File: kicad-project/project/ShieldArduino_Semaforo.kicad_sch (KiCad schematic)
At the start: 65 parts, among them IC2 TPS563200DDCR, J1 Conn_01x15, K1 RELAY, P1 Power, P2 Analog, P3 Digital, P4 Digital, P5 CONN_01X01, P6 CONN_01X01, P7 CONN_01X01, P8 CONN_01X01, Q1 PMOS, Q2 NMOS, Q3 NMOS, Q4 NMOS, Q5 NMOS, U1 MCP2542FD-E/MF, U2 LM321

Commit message: kicad-pcb-layout-v1.0
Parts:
- removed J1: Conn_01x15, footprint:L17HTHES4R1C, symbol Connector_Generic:Conn_01x15
- added J2: Conn_01x18, footprint:M80-54016YY, symbol Connector_Generic:Conn_01x18
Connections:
- net  relay_in: now also J2.6 (Pin_6)
- net +5V: now also J2.13 (Pin_13), J2.16 (Pin_16)
- net 12V_in: now also J2.1 (Pin_1)
- net EX_CAN+: now also J2.7 (Pin_7)
- net EX_CAN-: now also J2.8 (Pin_8)
- net GND: now also J2.10 (Pin_10), J2.15 (Pin_15), J2.17 (Pin_17), J2.18 (Pin_18), J2.9 (Pin_9)
- net brake_in: now also J2.14 (Pin_14)
- net high_speed: now also J2.12 (Pin_12)
- net inverter_signal_5V: now also J2.5 (Pin_5)
- net low_speed: now also J2.4 (Pin_4)
- net relay_out: now also J2.2 (Pin_2)
- net reverse: now also J2.3 (Pin_3)
- net throttle_in: now also J2.11 (Pin_11)
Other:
- moved on the sheet: D1, D11, D12, D13, D2, D3, D4

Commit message: kicad-pcb-layout-v1.0.1
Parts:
- added C3: 100n, Capacitor_SMD:C_0805_2012Metric_Pad1.18x1.45mm_HandSolder, symbol Device:C_Small
- added C5: 220p, Capacitor_SMD:C_0805_2012Metric_Pad1.18x1.45mm_HandSolder, symbol Device:C_Small
- added D6: D_Small, footprint:SODFL3618X100N, symbol Device:D_Small
- added IC1: TLIN1039DDFRQ1, SOT65P280X110-8N, symbol TLIN1039DDFRQ1:TLIN1039DDFRQ1
- added R12: 10k, Resistor_SMD:R_0805_2012Metric_Pad1.20x1.40mm_HandSolder, symbol Device:R_Small
- added R13: 1k, Resistor_SMD:R_0805_2012Metric_Pad1.20x1.40mm_HandSolder, symbol Device:R_Small
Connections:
- net +3V3: now also R12.1
- net 12V_in_protected: now also C3.1, D6.2 (A), IC1.7 (VSUP)
- net A4(SDA): now also J2.17 (Pin_17)
- net A5(SCL): now also J2.18 (Pin_18)
- net GND: now also C3.2, C5.2, IC1.5 (GND); no longer J2.15 (Pin_15), J2.17 (Pin_17), J2.18 (Pin_18)
- net UART_RX: now also IC1.4 (TXD)
- net UART_TX: now also IC1.1 (RXD)
- new net: IC1.2 (EN), R12.2
- new net: D6.1 (K), R13.1
- new net TLIN: C5.1, IC1.6 (LIN), J2.15 (Pin_15), R13.2
- no-connect marks 5 -> 7

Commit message: kicad-pcb-layout-v1.0.2
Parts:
- removed R14, R16: 10k, Resistor_SMD:R_0603_1608Metric_Pad0.98x0.95mm_HandSolder, symbol Device:R_Small
- removed R19: 5.2K, Resistor_SMD:R_0603_1608Metric_Pad0.98x0.95mm_HandSolder, symbol Device:R_Small
- removed U2: LM321, Package_TO_SOT_SMD:SOT-23-5, symbol Amplifier_Operational:LM321
- added C6: 100n, Capacitor_SMD:C_0805_2012Metric_Pad1.18x1.45mm_HandSolder, symbol Device:C_Small
- added IC3: MCP4901T-E_MS, SOP65P490X110-8N, symbol MCP4901T-E_MS:MCP4901T-E_MS
- added JP1: Jumper_2_Small_Bridged, symbol Jumper:Jumper_2_Small_Bridged
- added JP2: Jumper_2_Small_Open, symbol Jumper:Jumper_2_Small_Open
- added R21: 200, Resistor_SMD:R_0603_1608Metric_Pad0.98x0.95mm_HandSolder, symbol Device:R_Small
- added R22, R23: 5k, Resistor_SMD:R_0603_1608Metric_Pad0.98x0.95mm_HandSolder, symbol Device:R_Small
- added U3: LM4040DBZ-2.0, Package_TO_SOT_SMD:SOT-23, symbol Reference_Voltage:LM4040DBZ-2.0
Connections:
- net +3V3: now also R23.1
- net +5V: now also C6.1, IC3.1 (VDD)
- net 11(**/MOSI): now also IC3.4 (SDI)
- net 13(SCK): now also IC3.3 (SCK)
- net AREF: now also JP2.2 (B)
- net GND: now also C6.2, IC3.7 (VSS), R21.2, R22.2, U3.2 (A)
- net inverter_signal_5V: now also IC3.8 (VOUT)
- net 6(**) renamed STM_DAC_IN
- net STM_DAC_IN: now also IC3.2 (~{CS}), R21.1
- net 7 renamed STM_LDAC
- net STM_LDAC: now also IC3.5 (~{LDAC}), R22.1
- new net: IC3.6 (VREF), JP1.1 (A), JP2.1 (A)
- new net: JP1.2 (B), R23.2, U3.1 (K)
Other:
- note added: "DAC"
- note added: "PEDALS"
- note added: "TLIN"
- note removed: "OPAMP_ENG"
- note removed: "PEDAL"
- moved on the sheet: C3, C5, C7, D6, F2, IC1, P1, P2, P3, P4, P5, P6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

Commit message: kicad-pcb-layout-v1.0.4
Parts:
- JP1: footprint (none) -> Jumper:SolderJumper-2_P1.3mm_Bridged_RoundedPad1.0x1.5mm
- JP2: footprint (none) -> Jumper:SolderJumper-2_P1.3mm_Open_RoundedPad1.0x1.5mm
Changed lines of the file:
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@@
 		(on_board yes)
 		(dnp no)
-		(fields_autoplaced yes)
 		(property "Reference" "R23"
 			(at 218.44 41.9099 0)
@@
 			)
 		)
-		(property "Footprint" ""
+		(property "Footprint" "Jumper:SolderJumper-2_P1.3mm_Open_RoundedPad1.0x1.5mm"
 			(at 200.66 64.77 0)
 			(effects
@@
 			)
 		)
-		(property "Footprint" ""
+		(property "Footprint" "Jumper:SolderJumper-2_P1.3mm_Bridged_RoundedPad1.0x1.5mm"
 			(at 200.66 49.53 0)
 			(effects

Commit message: kicad-pcb-layout-v1.0.7
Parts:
- removed F2: 0.5A, Fuse:Fuse_1206_3216Metric_Pad1.42x1.75mm_HandSolder, symbol Device:Fuse_Small
- added F1: 3A, Fuse:Fuse_0603_1608Metric_Pad1.05x0.95mm_HandSolder, symbol Device:Fuse_Small
- D16: footprint Diode_SMD:D_SOD-323F -> Diode_SMD:D_SOD-323_HandSoldering
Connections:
- net 12V_in_protected: now also F1.2
- net at D9.1 (K), Q1.3 (S): now also F1.1
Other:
- note added: "current limiting resistor"
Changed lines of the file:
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@@
 		)
 	)
+	(text "current limiting resistor"
+		(exclude_from_sim no)
+		(at 202.692 180.34 0)
+		(effects
+			(font
+				(face "Calibri")
+				(size 1.016 1.016)
+			)
+		)
+	)
 	(text "1"
 		(exclude_from_sim no)
@@
 		)
 	)
+	(text "current limiting resistor"
+		(exclude_from_sim no)
+		(at 274.828 176.276 0)
+		(effects
+			(font
+				(face "Calibri")
+				(size 1.016 1.016)
+			)
+		)
+	)
 	(text "POWER SUPPLY UNIT"
 		(exclude_from_sim no)
@@
 		)
 	)
+	(text "current limiting resistor"
+		(exclude_from_sim no)
+		(at 125.984 180.594 0)
+		(effects
+			(font
+				(face "Calibri")
+				(size 1.016 1.016)
+			)
+		)
+	)
 	(text "CAN\n"
 		(exclude_from_sim no)
@@
 			)
 		)
-		(property "Footprint" "Diode_SMD:D_SOD-323F"
+		(property "Footprint" "Diode_SMD:D_SOD-323_HandSoldering"
 			(at 44.45 127 0)
 			(effects
@@
 	)
 	(symbol
+		(lib_id "Device:Fuse_Small")
+		(at 64.77 66.04 0)
+		(unit 1)
+		(exclude_from_sim no)
+		(in_bom yes)
+		(on_board yes)
+		(dnp no)
+		(fields_autoplaced yes)
+		(property "Reference" "F1"
+			(at 64.77 60.96 0)
+			(effects
+				(font
+					(size 1.27 1.27)
+				)
+				(hide yes)
+			)
+		)
+		(property "Value" "3A"
+			(at 64.77 63.5 0)
+			(effects
+				(font
+					(size 1.27 1.27)
+				)
+			)
+		)
+		(property "Footprint" "Fuse:Fuse_0603_1608Metric_Pad1.05x0.95mm_HandSolder"
+			(at 64.77 66.04 0)
+			(effects
+				(font
+					(size 1.27 1.27)
+				)
+				(hide yes)
+			)
+		)
+		(property "Datasheet" "https://www.mouser.pl/ProductDetail/Bourns/SF-0603FP300F-2?qs=55YtniHzbhAz28pQ%252B5v2Gg%3D%3D"
+			(at 64.77 66.04 0)
+			(effects
+				(font
+					(size 1.27 1.27)
+				)
+				(hide yes)
+			)
+		)
+		(property "Description" "Fuse, small symbol"
+			(at 64.77 66.04 0)
+			(effects
+				(font
+					(size 1.27 1.27)
+				)
+				(hide yes)
+			)
+		)
+		(pin "1"
+		)
+		(pin "2"
+		)
+		(instances
+			(project "ShieldArduino_Semaforo"
+				(path "/9ffb0a36-b6c4-4251-92f7-01d561ef1727"
+					(reference "F1")
+					(unit 1)
+				)
+			)
+		)
+	)
+	(symbol
 		(lib_id "Device:R_Small")
 		(at 76.2 34.29 0)
@@
 					(unit 1)
 				)
-			)
-		)
-	)
-	(symbol
-		(lib_id "Device:Fuse_Small")
-		(at 64.77 66.04 0)
-		(unit 1)
-		(exclude_from_sim no)
-		(in_bom yes)
-		(on_board yes)
-		(dnp no)
-		(fields_autoplaced yes)
-		(property "Reference" "F2"
-			(at 64.77 60.96 0)
-			(effects
-				(font
-					(size 1.27 1.27)
-				)
-			)
-		)
-		(property "Value" "0.5A"
-			(at 64.77 63.5 0)
-			(effects
-				(font
-					(size 1.27 1.27)
-				)
-			)
-		)
-		(property "Footprint" "Fuse:Fuse_1206_3216Metric_Pad1.42x1.75mm_HandSolder"
-			(at 64.77 66.04 0)
-			(effects
-				(font
-					(size 1.27 1.27)
-				)
-				(hide yes)
-			)
-		)
-		(property "Datasheet" "https://www.mouser.pl/ProductDetail/Eaton-Electronics/PTSAHT120624V050?qs=sGAEpiMZZMt8Ji9PfVTQzDC%2FQhf%2F9COsTqlHB7vDZt22fVe0wfbojQ%3D%3D"
-			(at 64.77 66.04 0)
-			(effects
-				(font
-					(size 1.27 1.27)
-				)
-				(hide yes)
-			)
-		)
-		(property "Description" "Fuse, small symbol"
-			(at 64.77 66.04 0)
-			(effects
-				(font
-					(size 1.27 1.27)
-				)
-				(hide yes)
-			)
-		)
-		(pin "1"
-		)
-		(pin "2"
-		)
-		(instances
-			(project "ShieldArduino_Semaforo"
-				(path "/9ffb0a36-b6c4-4251-92f7-01d561ef1727"
-					(reference "F2")
-					(unit 1)
-				)

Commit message: kicad-pcb-layout-v1.0.8
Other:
- note added: "PSU: PRZED PRZETWORNICA 1A BEZPIECZNIK"
- note added: "TVS: DODAĆ TVS NA I2C"
- note removed: "FARDRIVER: jakie piny potrzeba,do czego podłączać = ile tranzystorów bezpiecznik topikowy na zasilanie przekaźników/przekaźników przekaznik ON/OFF tranzystor REVERSE tranzystor 3 grade speed (highspeed, medium speed, lowspeed)"
- note removed: "PSU: ułożyć zasilacz tak jak na layout example (click+D) CHYBA GIT POTWIERDZIC Z WIKTOREM <3"
- note removed: "TVS: kazdy pinout musi miec tvs dobranego na working voltage +0.5V"
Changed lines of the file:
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@@
 		)
 	)
-	(text "PSU:\n	ułożyć zasilacz tak jak na layout example (click+D)\n	CHYBA GIT POTWIERDZIC Z WIKTOREM <3"
+	(text "PSU:\n	PRZED PRZETWORNICA 1A BEZPIECZNIK\n"
 		(exclude_from_sim no)
-		(at 17.78 -17.526 0)
+		(at 20.574 -26.416 0)
 		(effects
 			(font
@@
 		)
 	)
-	(text "FARDRIVER:\n	jakie piny potrzeba,do czego podłączać = ile tranzystorów\n	bezpiecznik topikowy na zasilanie przekaźników/przekaźników\n 	przekaznik ON/OFF\n	tranzystor REVERSE\n	tranzystor 3 grade speed (highspeed, medium speed, lowspeed)\n \n\n"
-		(exclude_from_sim no)
-		(at 17.78 -30.48 0)
-		(effects
-			(font
-				(size 1.27 1.27)
-			)
-			(justify left)
-		)
-	)
 	(text "ESD PROTECTION\n"
 		(exclude_from_sim no)
@@
 		)
 	)
-	(text "TVS:\n	kazdy pinout musi miec tvs dobranego na working voltage +0.5V\n\n"
+	(text "TVS:\n	DODAĆ TVS NA I2C\n\n"
 		(exclude_from_sim no)
-		(at 18.034 -22.606 0)
+		(at 20.828 -31.496 0)
 		(effects
 			(font
@@
 	(wire
 		(pts
-			(xy 134.62 186.69) (xy 134.62 187.96)
-		)
-		(stroke
-			(width 0)
-			(type default)
-		)
-	)
-	(wire
-		(pts
 			(xy 275.59 166.37) (xy 283.21 166.37)
 		)
@@
 	(symbol
 		(lib_id "power:GND")
-		(at 134.62 187.96 0)
+		(at 134.62 186.69 0)
 		(unit 1)
 		(exclude_from_sim no)
@@
 		(dnp no)
 		(property "Reference" "#PWR024"
-			(at 134.62 194.31 0)
+			(at 134.62 193.04 0)
 			(effects
 				(font
@@
 		)
 		(property "Value" "GND"
-			(at 134.874 192.532 0)
+			(at 134.874 191.262 0)
 			(effects
 				(font
@@
 		)
 		(property "Footprint" ""
-			(at 134.62 187.96 0)
+			(at 134.62 186.69 0)
 			(effects
 				(font
@@
 		)
 		(property "Datasheet" ""
-			(at 134.62 187.96 0)
+			(at 134.62 186.69 0)
 			(effects
 				(font
@@
 		)
 		(property "Description" "Power symbol creates a global label with name \"GND\" , ground"
-			(at 134.62 187.96 0)
+			(at 134.62 186.69 0)
 			(effects
 				(font

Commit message: kicad-pcb-layout-v1.0.9
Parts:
- added C8: 100n, Capacitor_SMD:C_0805_2012Metric_Pad1.18x1.45mm_HandSolder, symbol Device:C_Small
- added R14: 5k, Resistor_SMD:R_0603_1608Metric_Pad0.98x0.95mm_HandSolder, symbol Device:R_Small
- added R16: 10k, Resistor_SMD:R_0603_1608Metric_Pad0.98x0.95mm_HandSolder, symbol Device:R_Small
- added R19: 200, Resistor_SMD:R_0603_1608Metric_Pad0.98x0.95mm_HandSolder, symbol Device:R_Small
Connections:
- net A3: now also C8.1, R19.2
- net GND: now also C8.2, R16.2
- net inverter_signal_5V: now also R14.1
- new net: R14.2, R16.1, R19.1
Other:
- note added: "PSU: PRZED PRZETWORNICA 1A BEZPIECZNIK DAC: CZY A3 pin git?"
- note removed: "PSU: PRZED PRZETWORNICA 1A BEZPIECZNIK"

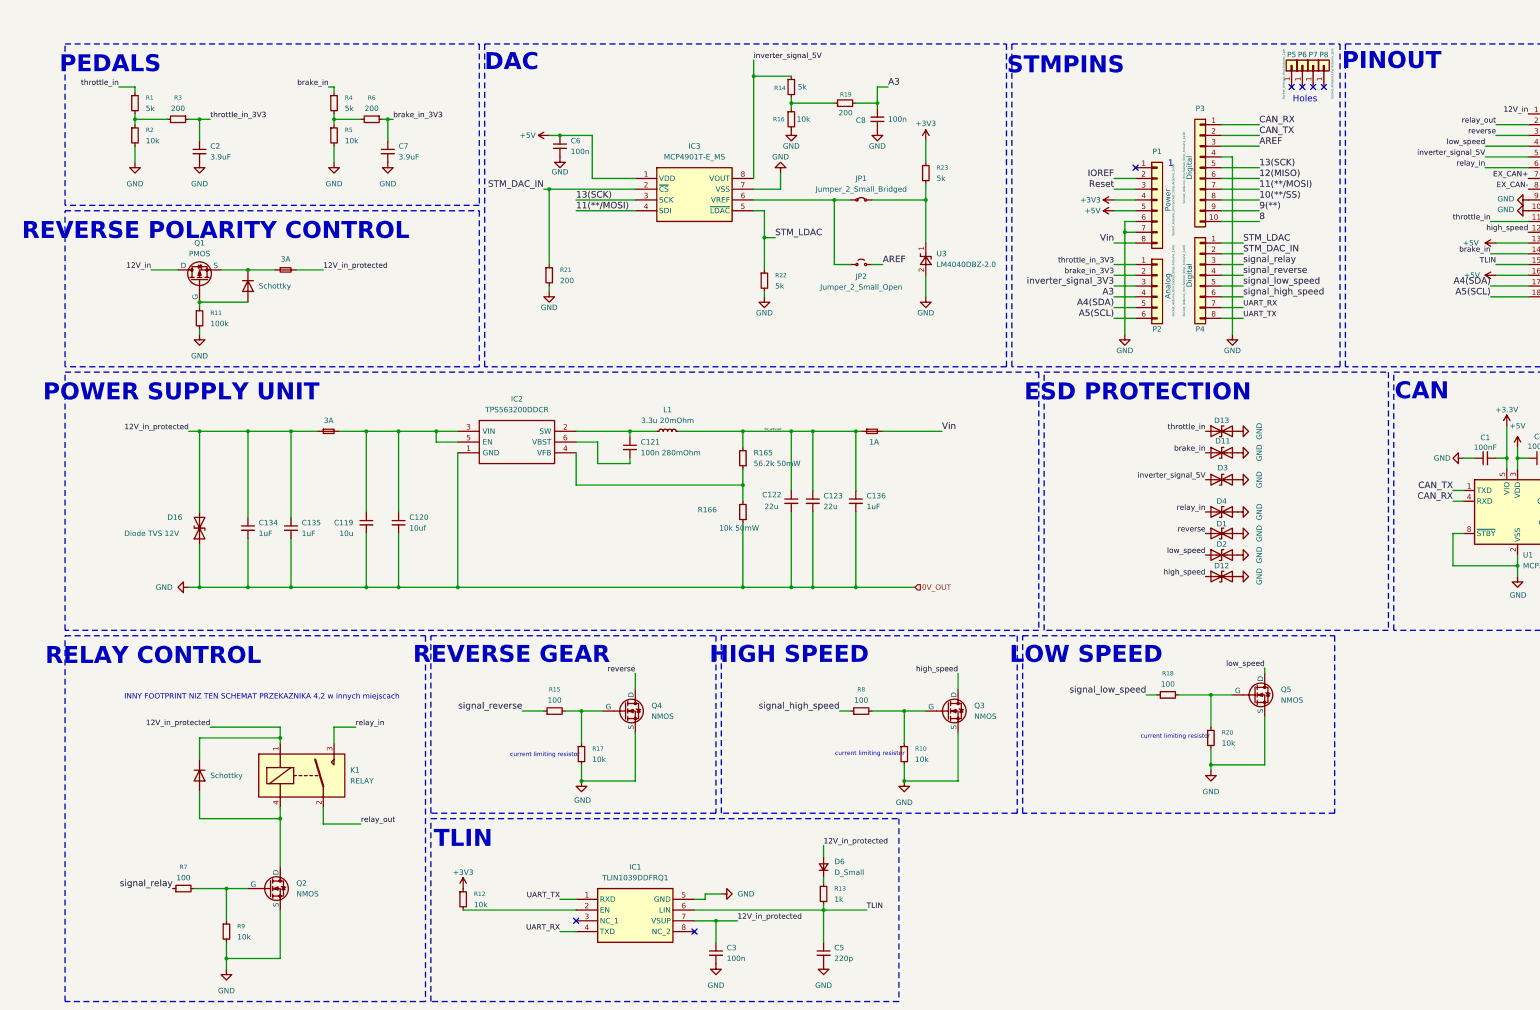
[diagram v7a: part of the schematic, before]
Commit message: Dodano test pointy na kazdym sensownym do pomiaru miejscu, dodano przelotki do masy - ground stitching
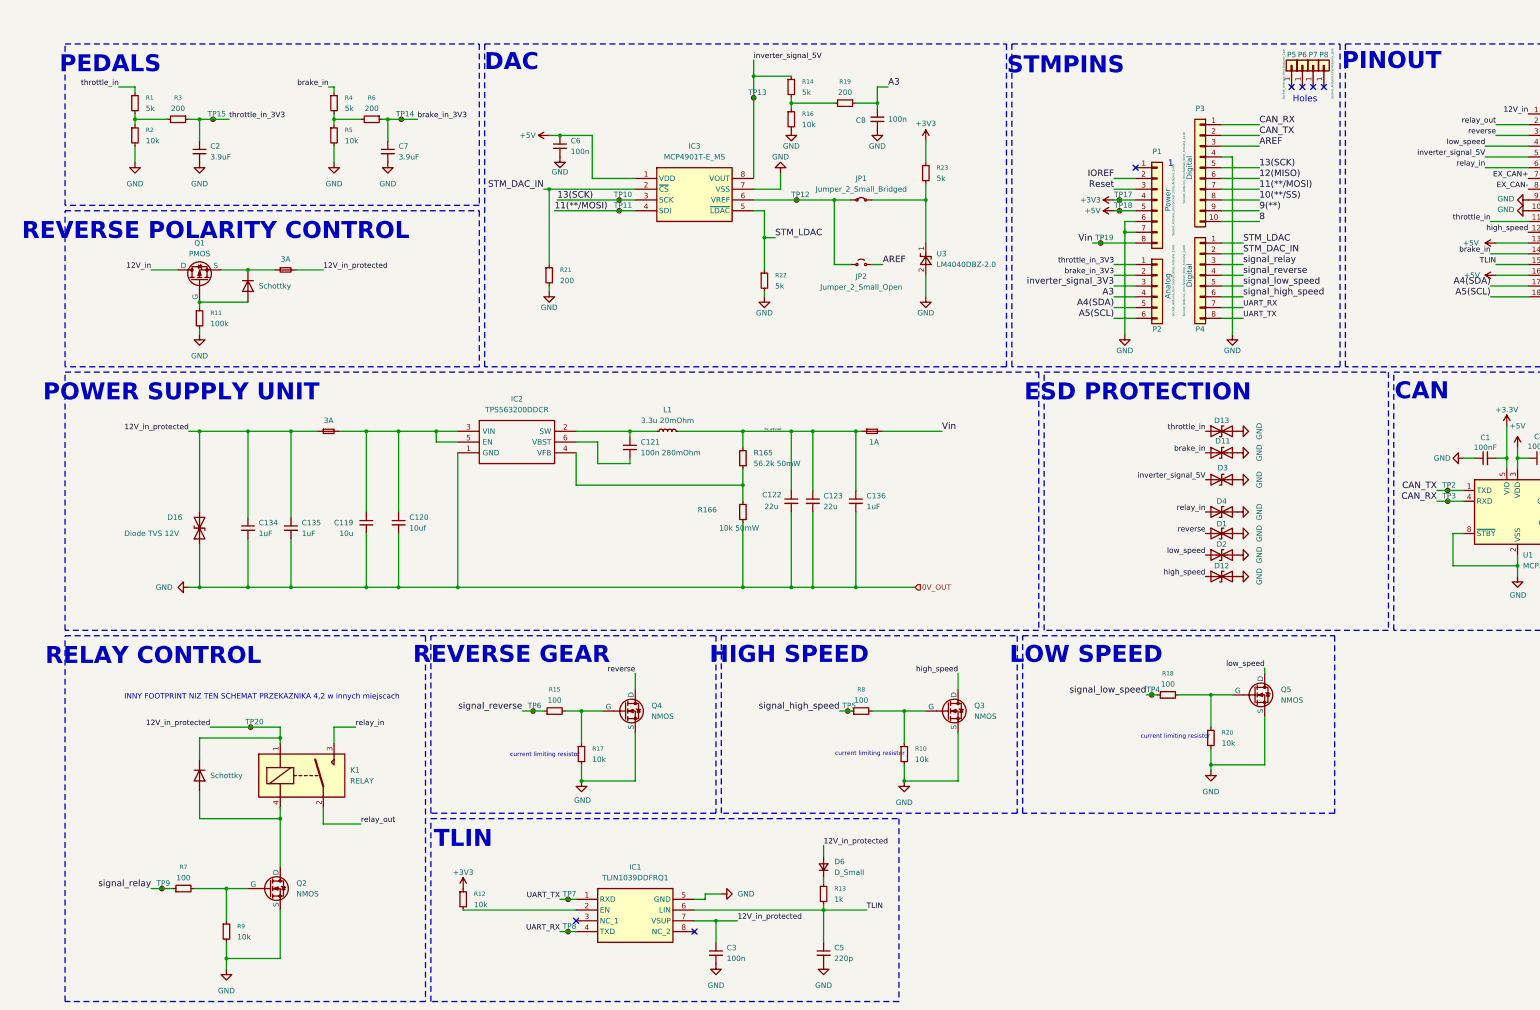
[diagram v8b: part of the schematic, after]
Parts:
- added TP10, TP11, TP12, TP13, TP14, TP15, TP17, TP18, TP19, TP2, TP20, TP3, TP4, TP5, TP6, TP7, TP8, TP9: TestPoint_Small, TestPoint:TestPoint_Pad_D1.5mm, symbol Connector:TestPoint_Small
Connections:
- net +3V3: now also TP17.1
- net +5V: now also TP18.1
- net 11(**/MOSI): now also TP11.1
- net 12V_in_protected: now also TP20.1
- net 13(SCK): now also TP10.1
- net A3: now also R19.1; no longer R19.2
- net CAN_RX: now also TP3.1
- net CAN_TX: now also TP2.1
- net UART_RX: now also TP8.1
- net UART_TX: now also TP7.1
- net Vin: now also TP19.1
- net brake_in_3V3: now also TP14.1
- net inverter_signal_5V: now also TP13.1
- net signal_high_speed: now also TP5.1
- net signal_low_speed: now also TP4.1
- net signal_relay: now also TP9.1
- net signal_reverse: now also TP6.1
- net throttle_in_3V3: now also TP15.1
- net at IC3.6 (VREF), JP1.1 (A), JP2.1 (A): now also TP12.1
- net at R14.2, R16.1: now also R19.2; no longer R19.1
